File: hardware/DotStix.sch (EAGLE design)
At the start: 29 parts, among them IC2 SI1145, U1 ATMEGA328P-MU-QFN32, U2 TMP102, U4 9DoF IMU

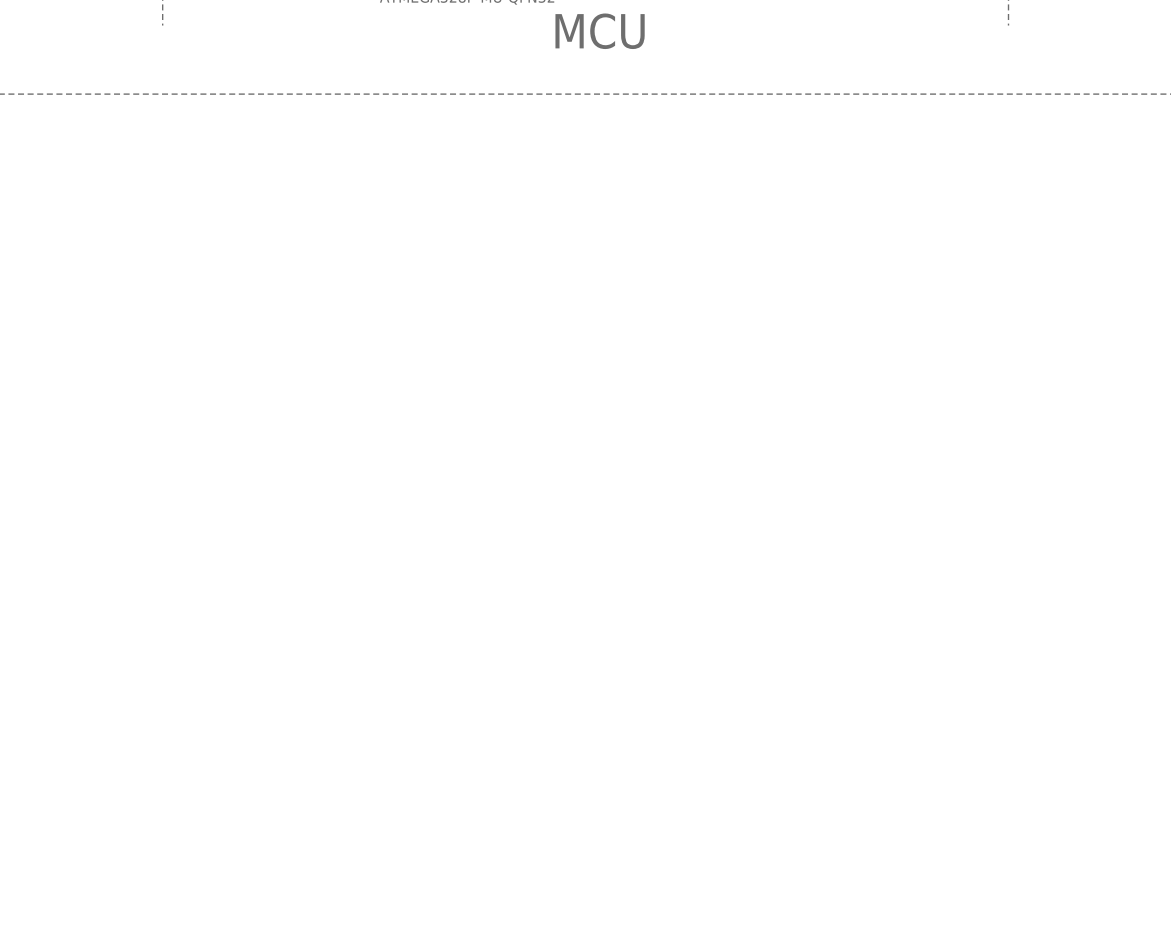
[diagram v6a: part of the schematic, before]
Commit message: Add 256kb EEPROM
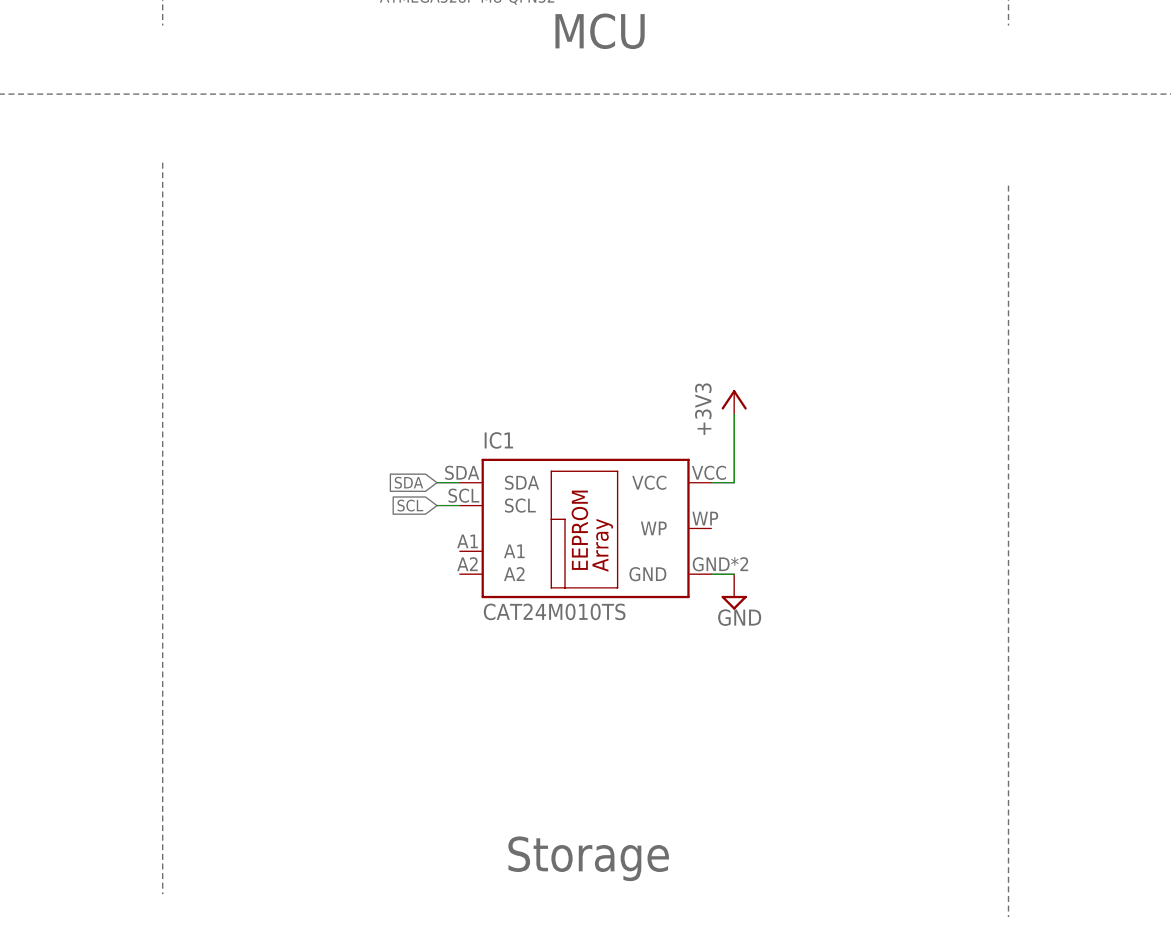
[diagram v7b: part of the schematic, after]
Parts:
- added IC1: CAT24M010TS, CAT24M01YI:CAT24M010TS
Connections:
- net +3V3: now also IC1.VCC
- net GND: now also IC1.GND
- net SCL: now also IC1.SCL
- net SDA: now also IC1.SDA
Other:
- note added: "Storage"
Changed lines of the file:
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@@
 <setting verticaltext="up"/>
 </settings>
-<grid distance="0.05" unitdist="inch" unit="inch" style="lines" multiple="1" display="no" altdistance="0.01" altunitdist="inch" altunit="inch"/>
+<grid distance="0.1" unitdist="inch" unit="inch" style="lines" multiple="1" display="no" altdistance="0.01" altunitdist="inch" altunit="inch"/>
 <layers>
 <layer number="1" name="Top" color="4" fill="1" visible="no" active="no"/>
@@
 <part name="SUPPLY28" library="supply2" deviceset="GND" device=""/>
 <part name="C1" library="rcl" deviceset="C-EU" device="C0201" value="0.1uF"/>
+<part name="SUPPLY9" library="supply2" deviceset="GND" device=""/>
+<part name="IC1" library="CAT24M01YI" deviceset="CAT24M01" device="TS" technology="0"/>
+<part name="+3V14" library="supply1" deviceset="+3V3" device=""/>
 </parts>
 <sheets>
@@
 <text x="69.85" y="81.28" size="1.778" layer="91">Using external weak pullup for really low current</text>
 <text x="407.67" y="171.45" size="1.016" layer="91" align="center">TMP102 or TMP112 (high acc +/-0.5°)</text>
+<wire x1="129.54" y1="-2.54" x2="129.54" y2="-83.82" width="0.1524" layer="95" style="longdash"/>
+<wire x1="223.52" y1="-5.08" x2="223.52" y2="-86.36" width="0.1524" layer="95" style="longdash"/>
+<text x="167.64" y="-81.28" size="3.81" layer="95">Storage</text>
 </plain>
 <instances>
@@
 <instance part="SUPPLY28" gate="GND" x="402.59" y="115.57"/>
 <instance part="C1" gate="G$1" x="407.67" y="118.11"/>
+<instance part="SUPPLY9" gate="GND" x="193.04" y="-50.8"/>
+<instance part="IC1" gate="G$1" x="175.26" y="-43.18"/>
+<instance part="+3V14" gate="G$1" x="193.04" y="-27.94"/>
 </instances>
 <busses>
@@
 <pinref part="C1" gate="G$1" pin="2"/>
 </segment>
+<segment>
+<pinref part="IC1" gate="G$1" pin="GND"/>
+<pinref part="SUPPLY9" gate="GND" pin="GND"/>
+<wire x1="190.5" y1="-48.26" x2="193.04" y2="-48.26" width="0.1524" layer="91"/>
+</segment>
 </net>
 <net name="SDA" class="0">
@@
 <wire x1="453.39" y1="120.65" x2="455.93" y2="120.65" width="0.1524" layer="91"/>
 <label x="455.93" y="120.65" size="1.27" layer="95" xref="yes"/>
+</segment>
+<segment>
+<wire x1="162.56" y1="-38.1" x2="160.02" y2="-38.1" width="0.1524" layer="91"/>
+<label x="160.02" y="-38.1" size="1.27" layer="95" rot="R180" xref="yes"/>
+<pinref part="IC1" gate="G$1" pin="SDA"/>
 </segment>
 </net>
@@
 <junction x="415.29" y="130.81"/>
 </segment>
+<segment>
+<wire x1="193.04" y1="-30.48" x2="193.04" y2="-38.1" width="0.1524" layer="91"/>
+<pinref part="IC1" gate="G$1" pin="VCC"/>
+<wire x1="193.04" y1="-38.1" x2="190.5" y2="-38.1" width="0.1524" layer="91"/>
+<pinref part="+3V14" gate="G$1" pin="+3V3"/>
+</segment>
 </net>
 <net name="MOSI" class="0">
@@
 <label x="455.93" y="123.19" size="1.27" layer="95" xref="yes"/>
 </segment>
-</net>
+<segment>
+<pinref part="IC1" gate="G$1" pin="SCL"/>
+<wire x1="162.56" y1="-40.64" x2="160.02" y2="-40.64" width="0.1524" layer="91"/>
+<label x="160.02" y="-40.64" size="1.27" layer="95" rot="R180" xref="yes"/>
+</segment>
+</net>

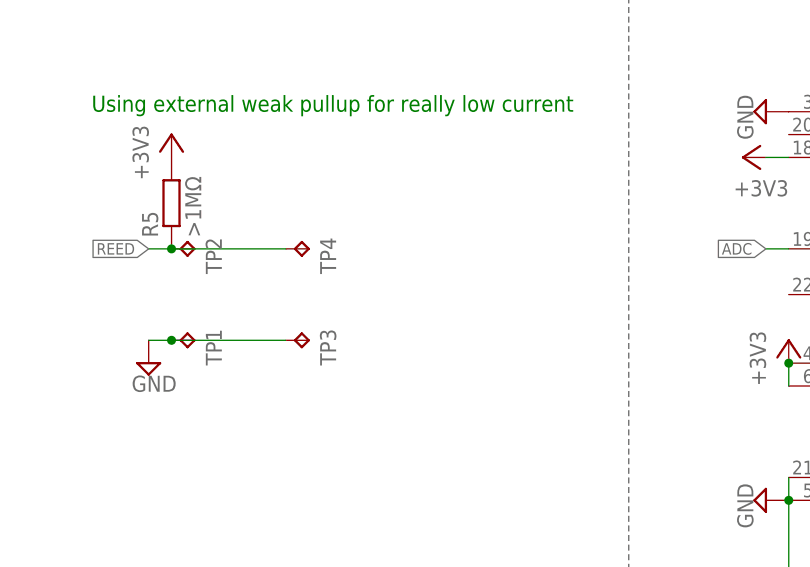
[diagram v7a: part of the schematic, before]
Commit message: Add reed switch for RST. Required for potting
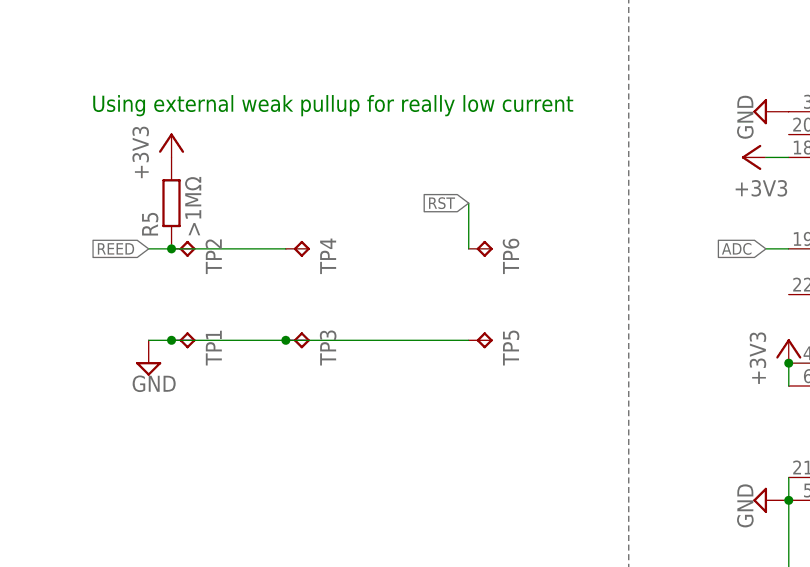
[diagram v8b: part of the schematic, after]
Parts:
- added TP5, TP6: TPTP20SQ, testpad:TPTP20SQ
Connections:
- net GND: now also TP5.TP
- net RST: now also TP6.TP
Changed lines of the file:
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@@
 <part name="IC1" library="CAT24M01YI" deviceset="CAT24M01" device="TS" technology="0"/>
 <part name="+3V14" library="supply1" deviceset="+3V3" device=""/>
+<part name="TP5" library="testpad" deviceset="TP" device="TP20SQ"/>
+<part name="TP6" library="testpad" deviceset="TP" device="TP20SQ"/>
 </parts>
 <sheets>
@@
 <instance part="IC1" gate="G$1" x="175.26" y="-43.18"/>
 <instance part="+3V14" gate="G$1" x="193.04" y="-27.94"/>
+<instance part="TP5" gate="G$1" x="114.3" y="55.88" rot="R270"/>
+<instance part="TP6" gate="G$1" x="114.3" y="66.04" rot="R270"/>
 </instances>
 <busses>
@@
 <wire x1="91.44" y1="55.88" x2="78.74" y2="55.88" width="0.1524" layer="91"/>
 <junction x="78.74" y="55.88"/>
+<pinref part="TP5" gate="G$1" pin="TP"/>
+<wire x1="111.76" y1="55.88" x2="91.44" y2="55.88" width="0.1524" layer="91"/>
+<junction x="91.44" y="55.88"/>
 </segment>
 <segment>
@@
 <wire x1="72.39" y1="148.59" x2="68.58" y2="148.59" width="0.1524" layer="91"/>
 </segment>
+<segment>
+<pinref part="TP6" gate="G$1" pin="TP"/>
+<wire x1="111.76" y1="66.04" x2="111.76" y2="71.12" width="0.1524" layer="91"/>
+<label x="111.76" y="71.12" size="1.27" layer="95" rot="R180" xref="yes"/>
+</segment>
 </net>
